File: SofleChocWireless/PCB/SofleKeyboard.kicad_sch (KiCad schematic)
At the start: 82 parts, among them J3 OLED_NICEVIEW_COMBO, SW1 SW_PUSH_LED, SW10 SW_PUSH_LED, SW11 SW_PUSH_LED, SW12 SW_PUSH_LED, SW13 SW_PUSH_LED, SW14 SW_PUSH_LED, SW15 SW_PUSH_LED, SW16 SW_PUSH_LED, SW17 SW_PUSH_LED, SW18 SW_PUSH_LED, SW19 SW_PUSH_LED, SW2 SW_PUSH_LED, SW20 SW_PUSH_LED, SW21 SW_PUSH_LED, SW22 SW_PUSH_LED, SW23 SW_PUSH_LED, SW24 SW_PUSH_LED, SW25 Rotary_Encoder_Switch, SW26 SW_PUSH_LED, SW27 SW_PUSH_LED, SW28 SW_PUSH_LED, SW29 SW_PUSH_LED, SW3 SW_PUSH_LED, SW30 SW_PUSH_LED, SW4 SW_PUSH_LED, SW5 SW_PUSH_LED, SW6 SW_PUSH_LED, SW7 SW_PUSH_LED, SW8 SW_PUSH_LED, SW9 SW_PUSH_LED, U1 ProMicro

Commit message: update pcb and schematic to fix parity issues
Update PCB and schematic to address differences between them
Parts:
- added JST_BATT2: Conn_01x02, SofleChoc:JST_PH_S2B-PH-K_1x02_P2.00mm_DoubleSided, symbol Connector_Generic:Conn_01x02
- added unit 1 of SW25
- added SW_BATT+2: SW_SPST, Button_Switch_SMD:SW_SPDT_PCM12, symbol Switch:SW_SPST
- J3: value OLED_NICEVIEW_COMBO -> OLED; footprint SofleChoc:PinHeader_1x05_P2.54mm_Vertical -> SofleChoc:OLED_NICEVIEW_COMBO_HDR_5Pin
- JP0, JP1, JP2, JP3, JP4, JP5, JP6, JP7, JP8, JP9: footprint SofleKeyboard-footprint:Jumper -> SofleChoc:Jumper_small
- SW1, SW13, SW19, SW7: footprint SofleChoc:Choc_Hotswap_SK6812MiniE -> SofleChoc:Choc_Hotswap_SK6812MiniE_BiggerHSPads_Column1
- SW10, SW11, SW12, SW14, SW15, SW16, SW17, SW18, SW2, SW20, SW21, SW22, SW23, SW24, SW26, SW27, SW28, SW29, SW3, SW30, SW4, SW5, SW6, SW8, SW9: footprint SofleChoc:Choc_Hotswap_SK6812MiniE -> SofleChoc:Choc_Hotswap_SK6812MiniE_BiggerHSPads
- SW25: value Rotary_Encoder_Switch -> SW_PUSH_LED; footprint SofleChoc:Kailh-PG1350-1u-reversible-SK6812MiniE -> SofleChoc:Kailh-PG1350-1u-reversible-SK6812MiniE_MODIFIED
- SW31: renamed from SW25; symbol SofleKeyboard-rescue:Rotary_Encoder_Switch-Device -> Device:RotaryEncoder_Switch
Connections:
- net DATA: now also U1.1 (TX(PD3)); no longer U1.2 (RX(PD2))
- net GND: now also JST_BATT2.1 (Pin_1)
- net LED: now also U1.2 (RX(PD2)); no longer U1.1 (TX(PD3))
- net at SW_BATT+1.1 (A), U1.24 (RAW): now also SW_BATT+2.1 (A)
- net at JST_BATT1.2 (Pin_2), SW_BATT+1.2 (B): now also JST_BATT2.2 (Pin_2), SW_BATT+2.2 (B)
- net SW25A renamed col5
- net col5: now also SW25.5
- net SW25B: no longer names the net of D25.2 (A), SW31.S2
- net SW25B: now also SW25.6

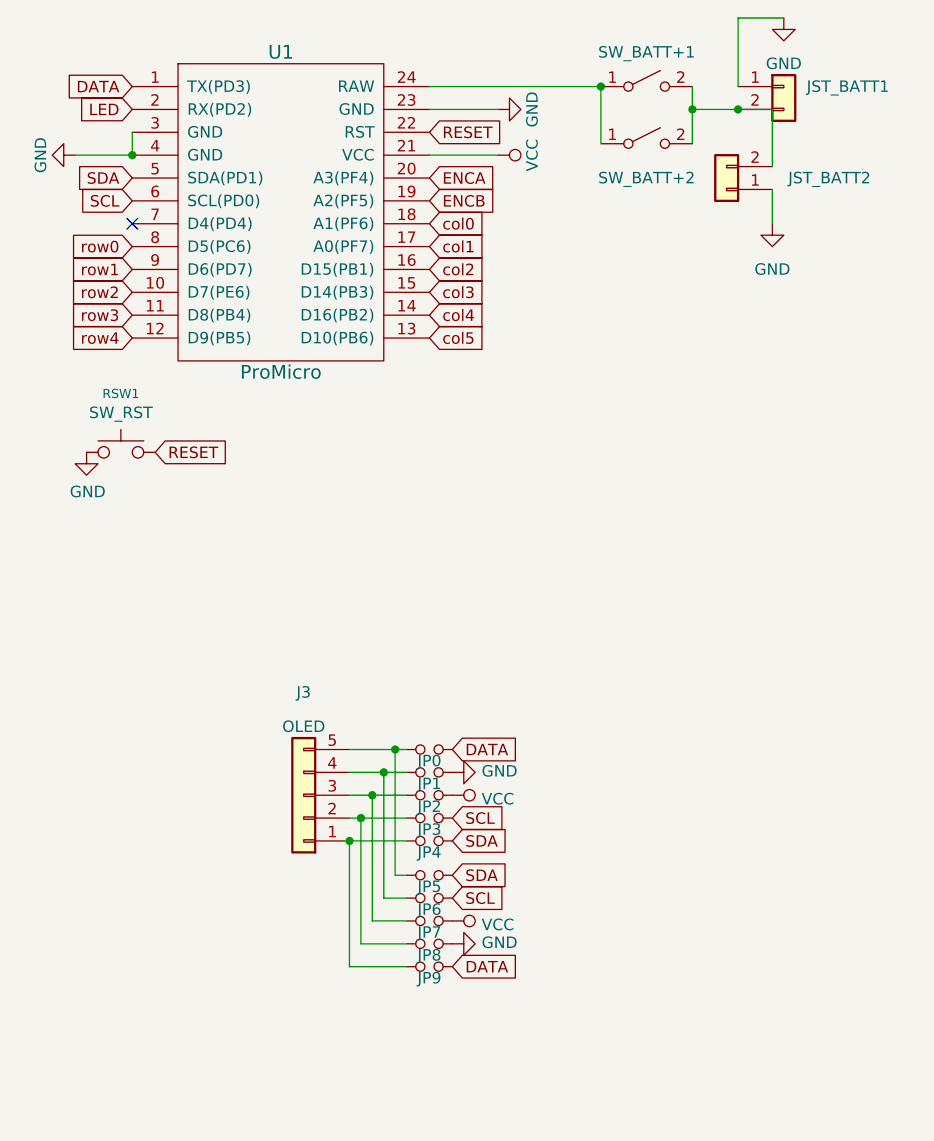
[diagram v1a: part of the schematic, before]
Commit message: update DATA net name to CS
CS corresponds to the chip select pin used by the nice!view display
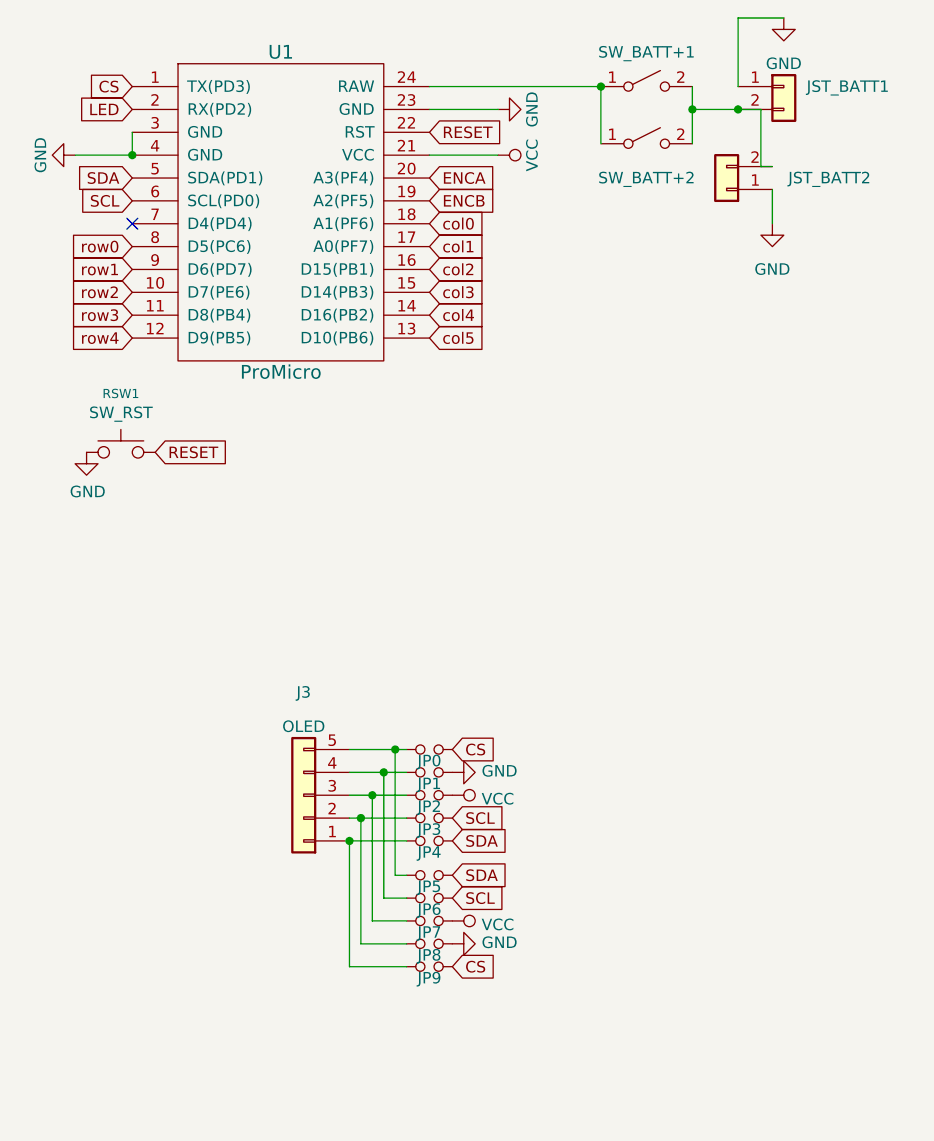
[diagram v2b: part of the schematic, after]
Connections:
- net DATA renamed CS
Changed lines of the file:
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@@
+    (stroke (width 0) (type default) (color 0 0 0 0))
+  )
+  (wire (pts (xy 97.79 30.48) (xy 99.06 30.48))
     (stroke (width 0) (type default) (color 0 0 0 0))
   )
@@
     (stroke (width 0) (type default) (color 0 0 0 0))
   )
-  (wire (pts (xy 95.25 24.13) (xy 99.06 24.13))
+  (wire (pts (xy 95.25 24.13) (xy 97.79 24.13))
     (stroke (width 0) (type default) (color 0 0 0 0))
   )
@@
     (stroke (width 0) (type default) (color 0 0 0 0))
   )
-  (wire (pts (xy 99.06 30.48) (xy 99.06 24.13))
+  (wire (pts (xy 97.79 30.48) (xy 97.79 24.13))
     (stroke (width 0) (type default) (color 0 0 0 0))
   )
@@
     )
   )
-  (global_label "DATA" (shape input) (at 63.5 95.25 0) (fields_autoplaced)
-    (effects (font (size 1.27 1.27)) (justify left))
-    (property "Intersheet References" "${INTERSHEET_REFS}" (id 0) (at 70.239 95.1706 0)
+  (global_label "CS" (shape input) (at 63.5 95.25 0) (fields_autoplaced)
+    (effects (font (size 1.27 1.27)) (justify left))
+    (property "Intersheet References" "${INTERSHEET_REFS}" (id 0) (at 68.3037 95.1706 0)
       (effects (font (size 1.27 1.27)) (justify left) hide)
     )
@@
     )
   )
-  (global_label "DATA" (shape input) (at 63.5 119.38 0) (fields_autoplaced)
-    (effects (font (size 1.27 1.27)) (justify left))
-    (property "Intersheet References" "${INTERSHEET_REFS}" (id 0) (at 70.239 119.3006 0)
+  (global_label "CS" (shape input) (at 63.5 119.38 0) (fields_autoplaced)
+    (effects (font (size 1.27 1.27)) (justify left))
+    (property "Intersheet References" "${INTERSHEET_REFS}" (id 0) (at 68.3037 119.3006 0)
       (effects (font (size 1.27 1.27)) (justify left) hide)
     )
@@
     )
   )
-  (global_label "DATA" (shape input) (at 27.94 21.59 180) (fields_autoplaced)
-    (effects (font (size 1.27 1.27)) (justify right))
-    (property "Intersheet References" "${INTERSHEET_REFS}" (id 0) (at 0 -2.54 0)
-      (effects (font (size 1.27 1.27)) hide)
-    )
-  )
+  (global_label "CS" (shape input) (at 27.94 21.59 180) (fields_autoplaced)
+    (effects (font (size 1.27 1.27)) (justify right))
+    (property "Intersheet References" "${INTERSHEET_REFS}" (id 0) (at 23.1363 21.5106 0)
+      (effects (font (size 1.27 1.27)) (justify right) hide)
+    )
+  )
